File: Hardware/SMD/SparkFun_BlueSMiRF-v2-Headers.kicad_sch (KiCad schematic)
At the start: 38 parts, among them J1 Conn_01x06, Q1 Q_NMOS_DGS, Q2 Q_NMOS_DGS, SW1 Switch, U1 ESP32_Pico_Mini, U2 AP2112K-3.3

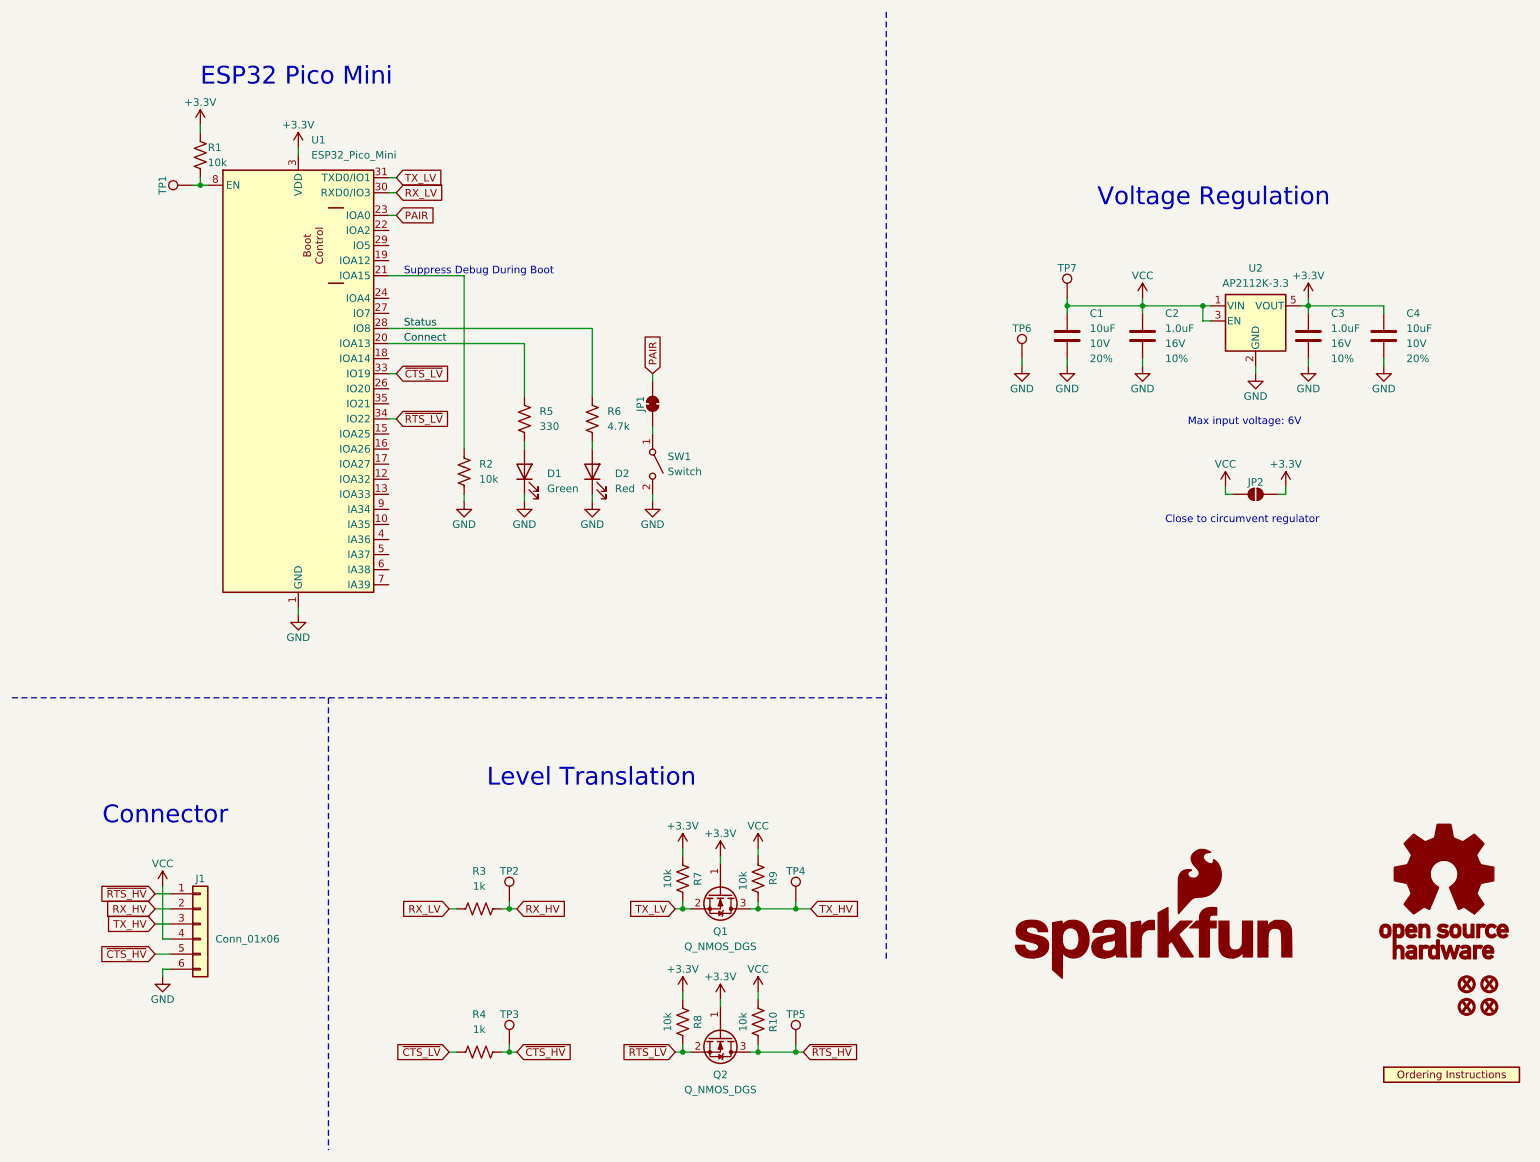
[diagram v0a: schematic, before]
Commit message: Rename Design Files
- The SMD is actually the one with the headers. =) Renaming files to reflect the boards with headers.
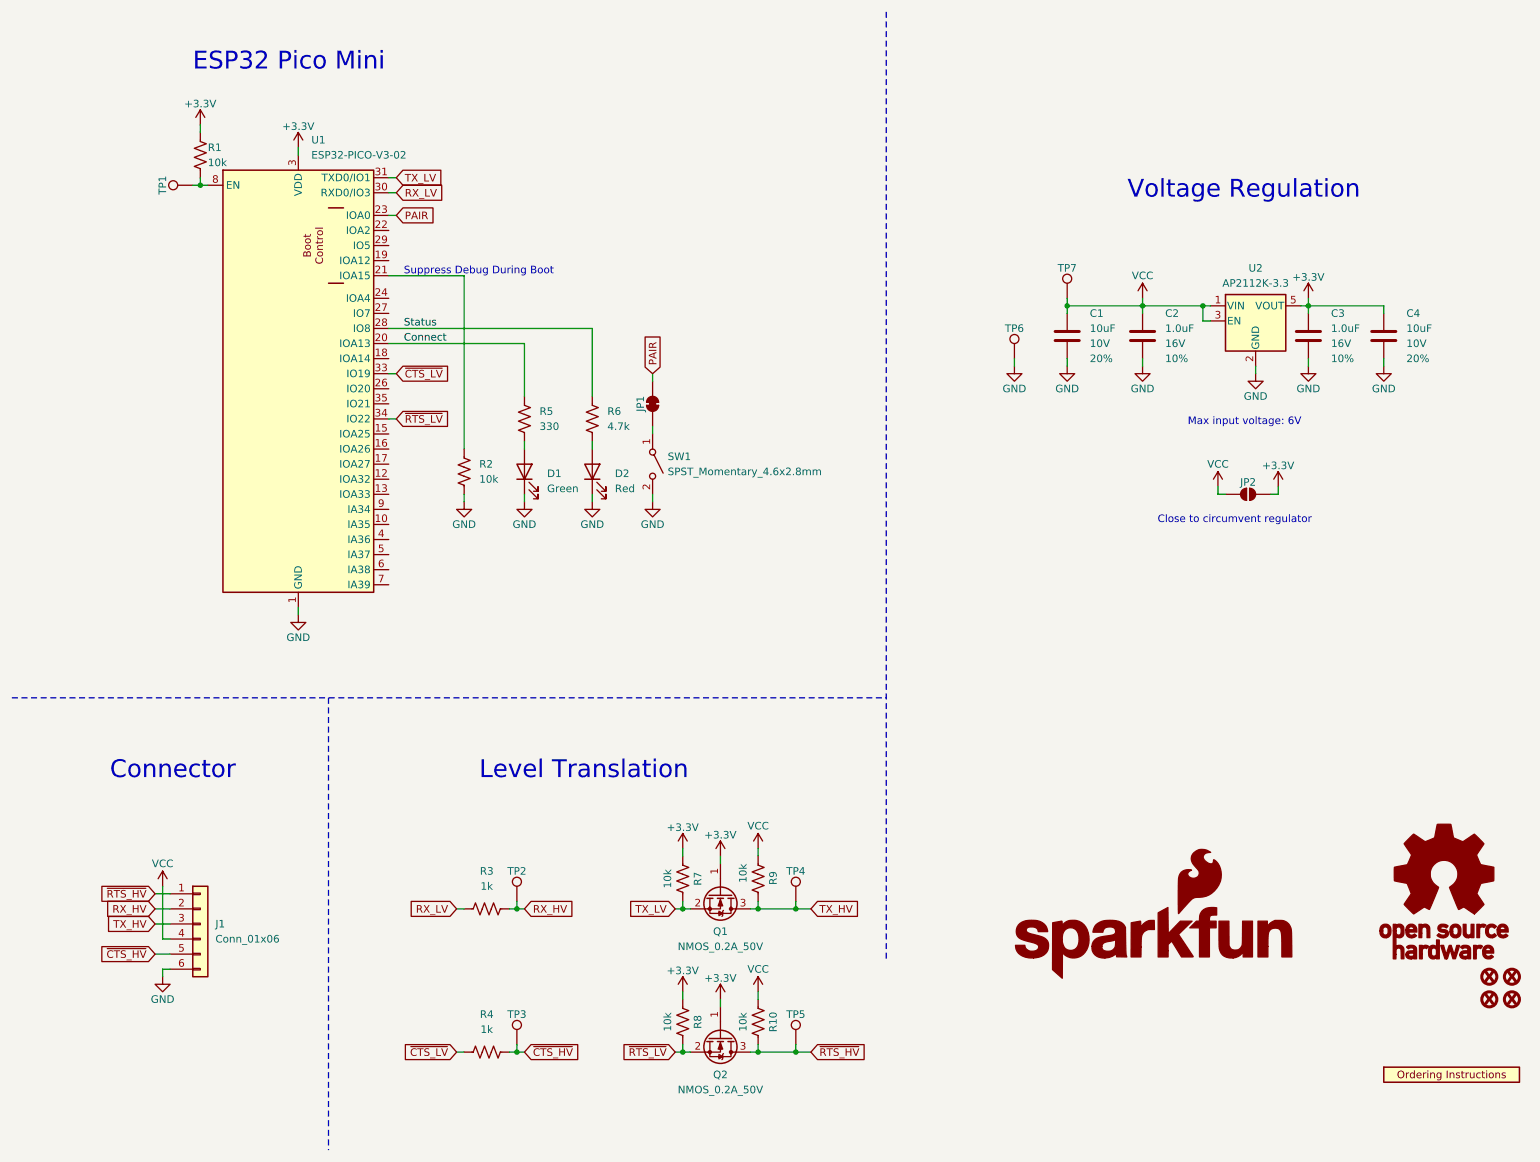
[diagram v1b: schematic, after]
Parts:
- removed J1: Conn_01x06, SparkFun-Connector:1X06, symbol SparkFun-Connector:Conn_01x06
- added J1: Conn_01x06, SparkFun-Connector:1X06-SMD_RA_MALE, symbol SparkFun-Connector:Conn_01x06_RA_SMD
- Q1, Q2: value Q_NMOS_DGS -> NMOS_0.2A_50V
- SW1: value Switch -> SPST_Momentary_4.6x2.8mm
- U1: value ESP32_Pico_Mini -> ESP32-PICO-V3-02
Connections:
- net GND: now also J1.6 (Pin_6)
- net RX_HV: now also J1.2 (Pin_2)
- net TX_HV: now also J1.3 (Pin_3)
- net VCC: now also J1.4 (Pin_4)
- net ~{CTS_HV}: now also J1.5 (Pin_5)
- net ~{RTS_HV}: now also J1.1 (Pin_1)
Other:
- title: SparkFun BlueSMiRF v2 - Headers -> SparkFun BlueSMiRF v2 Headers
- moved on the sheet: R3, R4

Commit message: Add 3D models
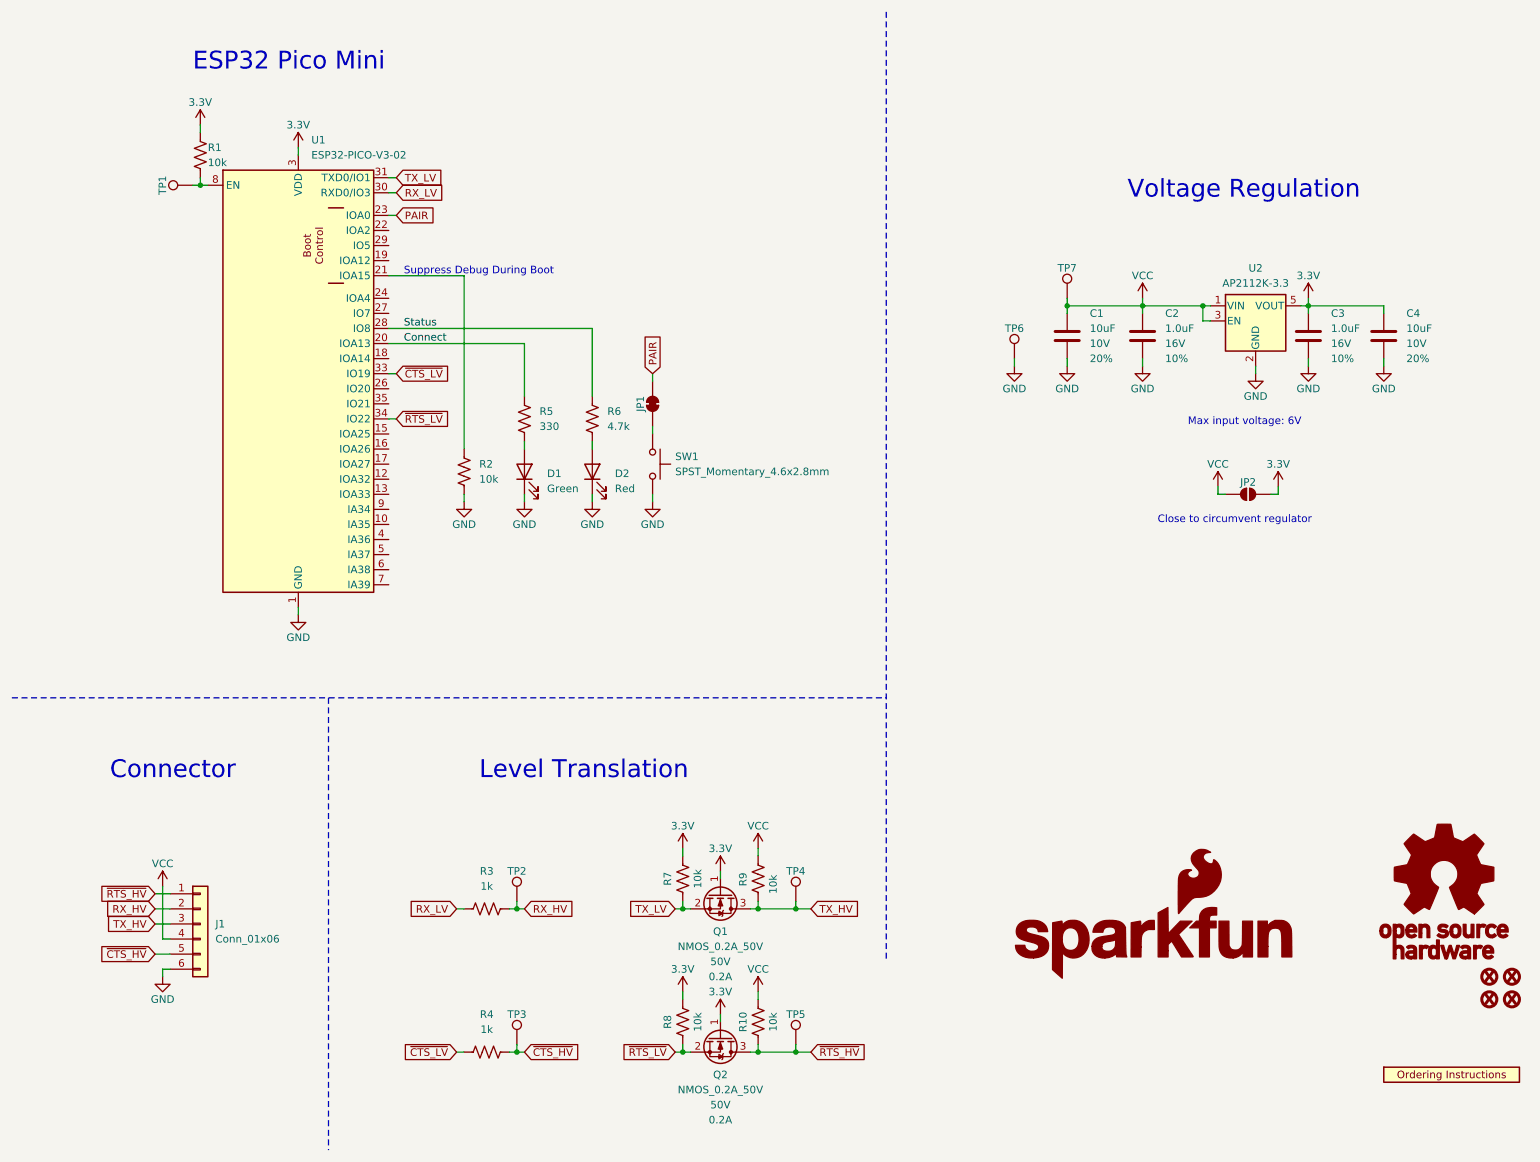
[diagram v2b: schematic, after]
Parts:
- D1: footprint SparkFun-LED:LED_0603_1608Metric -> SparkFun-LED:LED_0603_1608Metric_Green
- D2: footprint SparkFun-LED:LED_0603_1608Metric -> SparkFun-LED:LED_0603_1608Metric_Red
- FID1, FID2, FID3, FID4: symbol SparkFun-Aesthetic:Fiducial_0.5 -> SparkFun-Aesthetic:Fiducial_0.5mm
- J1: footprint SparkFun-Connector:1X06-SMD_RA_MALE -> SparkFun-Connector:1x06_SMD_RA_Male
- JP1: footprint SparkFun-Jumper:SMT-JUMPER_2_NC_TRACE_SILK -> SparkFun-Jumper:Jumper_2_NC_Trace
- JP2: footprint SparkFun-Jumper:SMT-JUMPER_2_NO_SILK -> SparkFun-Jumper:Jumper_2_NO
- Q1, Q2: IMax (none) -> 0.2A; VMax (none) -> 50V
- SW1: footprint SparkFun-Switch:Momentary_SMD_4.6x2.8mm -> SparkFun-Switch:Push_SMD_4.6x2.8mm_h2.5mm; symbol SparkFun-Switch:SPST_Momentary_4.6x2.8mm -> SparkFun-Switch:SPST_Push_SMD_4.6x2.8mm_h2.5mm
- TP1: footprint SparkFun-Connector:1X01 -> SparkFun-Connector:1x01
- U1: footprint SparkFun-RF:ESP32-MINI -> SparkFun-RF:ESP32-PICO-MINI
- U2: Imax (none) -> 600mA; Iq (none) -> 55µA; VMax (none) -> 6V
- U3: footprint SparkFun-Aesthetic:ORDERING_INSTRUCTIONS -> SparkFun-Aesthetic:Ordering_Instructions
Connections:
- net GND: now also R2.1; no longer R2.2
- net TX_HV: now also R9.1; no longer R9.2
- net TX_LV: now also R7.1; no longer R7.2
- net VCC: now also R10.2, R9.2; no longer R10.1, R9.1
- net ~{RTS_HV}: now also R10.1; no longer R10.2
- net ~{RTS_LV}: now also R8.1; no longer R8.2
- net at U1.21 (IOA15): now also R2.2; no longer R2.1
- net +3.3V renamed 3.3V
- net 3.3V: now also R7.2, R8.2; no longer R7.1, R8.1
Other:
- moved on the sheet: R10, R2, R3, R4, R5, R6, R7, R8, R9

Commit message: Update to use current SparkFun KiCad library
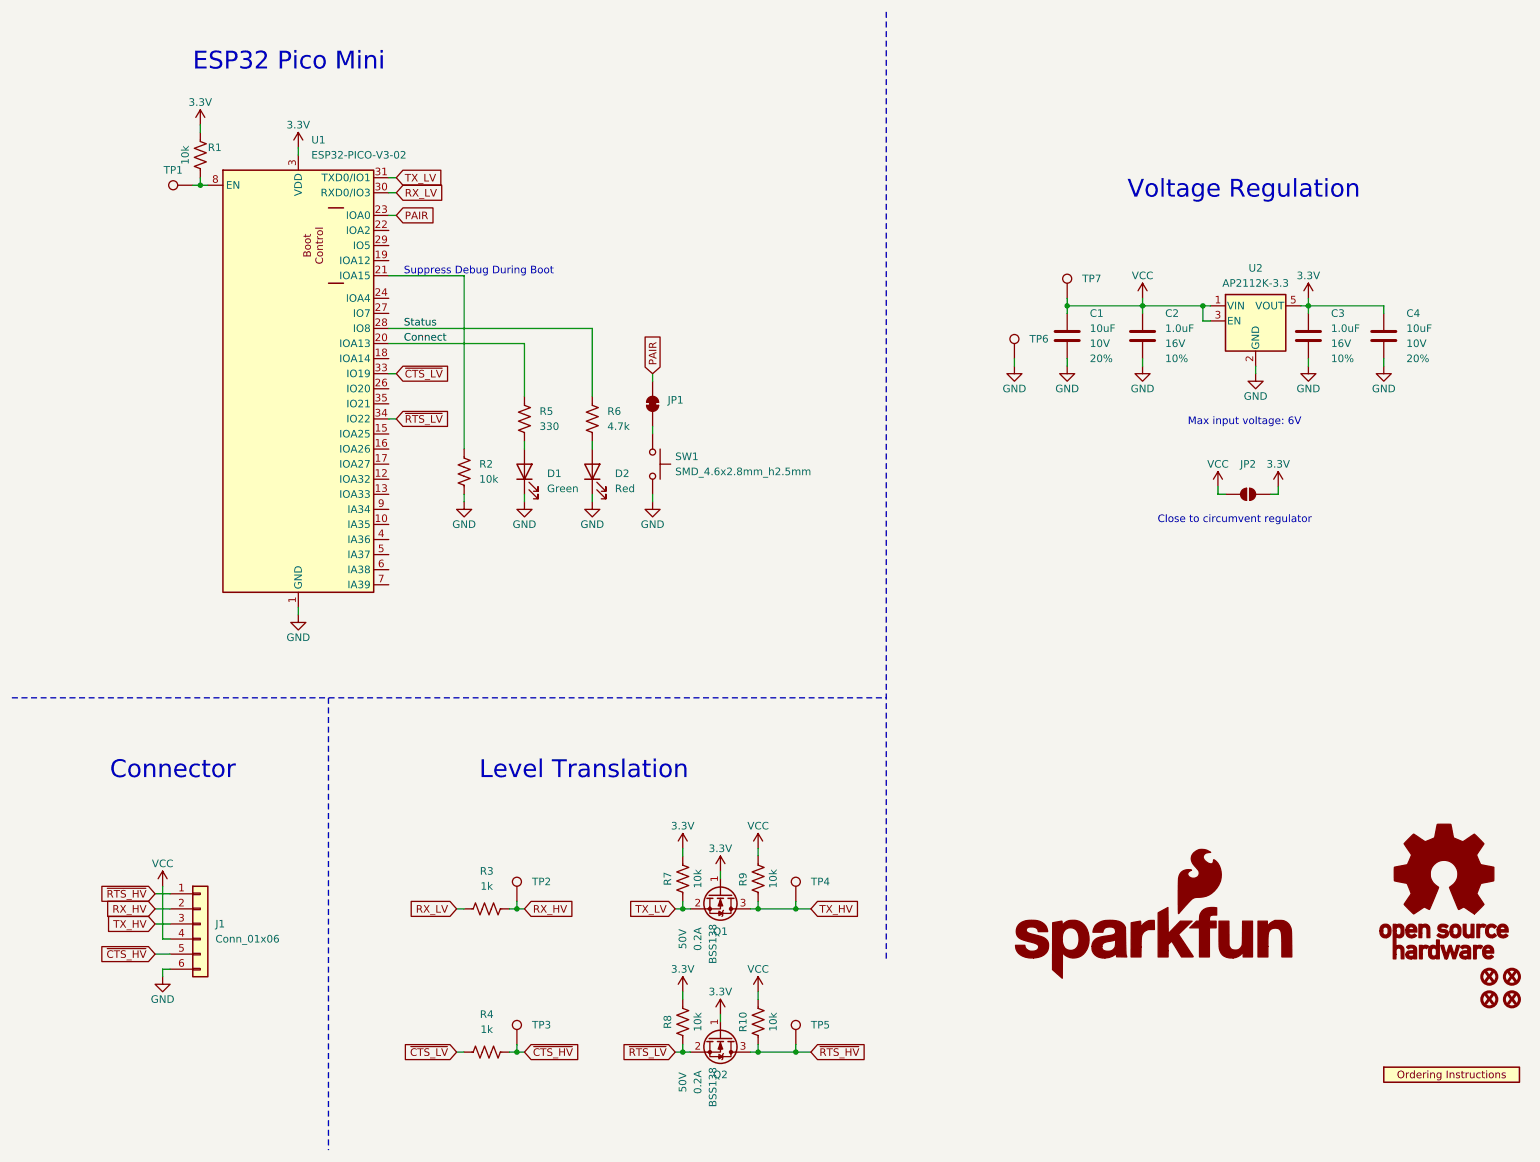
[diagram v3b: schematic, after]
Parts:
- FID1, FID2, FID3, FID4: value Fiducial_0.5 -> Fiducial_0.5mm
- Q1, Q2: value NMOS_0.2A_50V -> BSS138
- SW1: value SPST_Momentary_4.6x2.8mm -> SMD_4.6x2.8mm_h2.5mm
- TP1: value TestPoint -> PTH
- TP2, TP3, TP4, TP5, TP6, TP7: value TestPoint_0.75mm -> 0.75mm
